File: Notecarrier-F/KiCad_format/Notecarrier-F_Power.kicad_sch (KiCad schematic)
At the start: 0 parts

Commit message: Port Notecarrier-F schematic and BOM.
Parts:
- added C1, C11, C14, C15, C16, C17, C20: 10µF, symbol Device:C
- added C10, C18, C19, C21, C25, C3: 0.1µF, symbol Device:C
- added C12: 47µF, symbol Device:C
- added C13: 4.7µF, symbol Device:C
- added C2: 1µF, symbol Device:C
- added C22, C23, C24: 22µF, symbol Device:C_Small
- added C4: 10000pF, symbol Device:C
- added DS1, DS2, DS4, DS5: FSV1045V, blues-kicad-lib:TO277-3, symbol blues-kicad-lib:FSV1045V
- added DS3, DS6, DS7: STPS3H100U, symbol Device:D_Schottky_Filled
- added J1, J2, J3: S2BPHSM4TBLFSN, symbol Connector_Generic:Conn_01x02
- added J4: 10118193-0001LF, symbol Connector:USB_B_Micro
- added L1: XFL4020-222MEC, symbol Device:L
- added L2: 1.5uH, symbol Device:L
- added L3: 1285AS-H-2R2M=P2, symbol Device:L
- added R1, R2, R4: 10k, symbol Device:R
- added R13: 1.1M, symbol Device:R
- added R14: 180k, symbol Device:R
- added R16: 10MOhms, symbol Device:R
- added R17: 82kOhms, symbol Device:R
- added R3: 470R, symbol Device:R
- added R5: 1M, symbol Device:R
- added TVS1: SM6T6V8A, Diode_SMD:D_SMB, symbol Diode:SM6T6V8A
- added U1: TPS62748YFPT, blues-kicad-lib:XFBGA8, symbol blues-kicad-lib:TPS62748YFPT_NoLabel
- added U2: BQ24210DQCT, blues-kicad-lib:BQ24210DQCT, symbol blues-kicad-lib:BQ24210DQCT
- added U3: TPS63020DSJR, symbol blues-kicad-lib:TPS63020DSJR
- added U5: MAX17225ELT+, blues-kicad-lib:WDFN6-0200X0200, symbol blues-kicad-lib:MAX17225ELT_NoLabel
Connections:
- new net: L1.1, U5.2 (LX)
- new net: R17.1, U5.4 (SEL)
- new net: L2.1, U3.6 (L2-1), U3.7 (L2-2)
- new net: L2.2, U3.8 (L1-2), U3.9 (L1-1)
- new net: C18.1, U3.1 (VINA)
- new net: R3.1, U2.2 (ISET)
- new net: R4.1, U2.4 (VTSB), U2.5 (TS)
- new net: L3.2, U1.A1 (SW)
- new net: C22.1, C23.1, C24.1, C25.1, DS5.1 (A1), DS5.2 (A2), R13.1, U3.4 (VOUT), U3.5 (VOUT)
- new net: DS3.1 (K), DS4.3 (C), U2.1 (VBUS)
- new net: R13.2, R14.1, U3.3 (FB)
- new net: C4.1, J4.6 (Shield), R5.2
- new net: R2.2, U2.6 (~{PG}), U2.7 (~{EN})
- new net 1V8: C14.1, C15.1, C20.1, C21.1, L1.2, L3.1, U1.C2 (VOS), U5.5 (IN), U5.6 (EN)
- new net D_N: J4.2 (D-)
- new net D_P: J4.3 (D+)
- new net EN_F_BAT: U3.12 (EN)
- new net F_BAT: DS5.3 (C)
- new net F_VUSB: DS7.2 (A)
- new net GND: C1.2, C10.2, C11.2, C12.2, C13.2, C14.2, C15.2, C16.2, C17.2, C18.2, C19.2, C2.2, C20.2, C21.2, C22.2, C23.2, C24.2, C25.2, C3.2, C4.2, J1.1 (Pin_1), J2.1 (Pin_1), J3.1 (Pin_1), J4.5 (GND), R14.2, R17.2, R3.2, R4.2, R5.1, TVS1.2 (A2), U1.B2 (GND), U1.D1 (CTRL), U2.11 (EXP), U2.3 (VSS), U3.13 (PS/PSYNC), U3.15 (EXP), U3.2 (GND), U5.3 (GND)
- new net N_AUX5: R1.2, U2.8 (~{CHG})
- new net N_EN: C19.1, R16.2, U1.B1 (EN)
- new net N_VIO: C10.1, C11.1, R1.1, U5.1 (OUT)
- new net V+: DS1.1 (A1), DS1.2 (A2), J1.2 (Pin_2)
- new net VBAT: C2.1, DS2.1 (A1), DS2.2 (A2), J3.2 (Pin_2), R2.1, U2.10 (BAT)
- new net VMAIN: C12.1, C13.1, C16.1, C17.1, DS1.3 (C), DS2.3 (C), DS6.1 (K), DS7.1 (K), R16.1, TVS1.1 (A1), U1.A2 (VIN), U1.C1 (VSEL), U3.10 (VIN), U3.11 (VIN)
- new net VSOLAR: C1.1, DS4.1 (A1), DS4.2 (A2), J2.2 (Pin_2)
- new net VUSB: C3.1, DS3.2 (A), DS6.2 (A), J4.1 (VBUS)
- no-connect marks 0 -> 4
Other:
- note added: "1V8 Power Supply"
- note added: "Feather VBAT Power Supply"
- note added: "Isdmax=1uA"
- note added: "Li-po battery 3.3V - 4.2V"
- note added: "Li-po must be equal to or greater than 800mAh"
- note added: "Main Power Bus"
- note added: "Notecard USB"
- note added: "Notecard VIO Power Supply"
- note added: "Primary Battery"
- note added: "Primary Battery 2.5V - 4.2V"
- note added: "Riset = Kiset / Iiset where Kiset is 395 typically. With 470R --> 800mA"
- note added: "Solar"
- note added: "Solar panel connector"
- note added: "V+"
- title: (none) -> Notecarrier-F

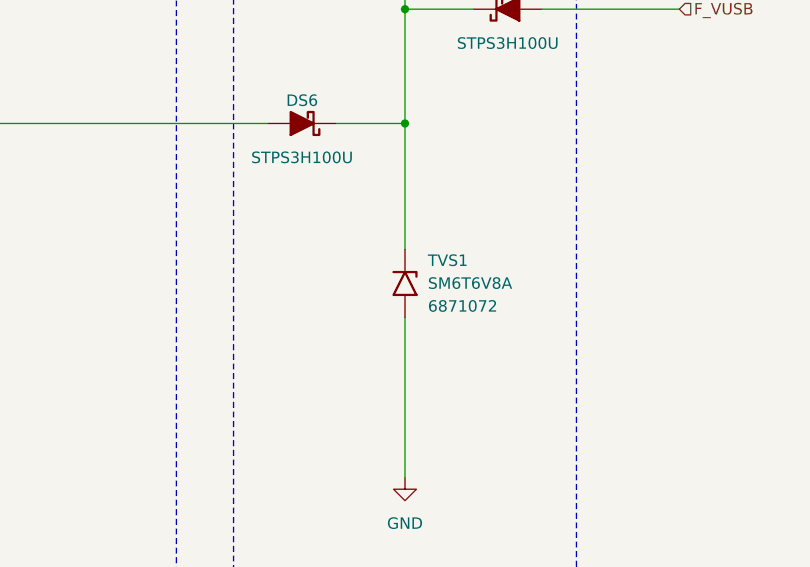
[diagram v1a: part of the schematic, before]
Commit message: Ported footprint assignments, board outline, copper layers and dimensional drawings for Notecarrier-F.
Footprints currently held in a “blues-kicad-lib-pending” library, prior to merging with “blues-kicad-lib” and deleting unused items.
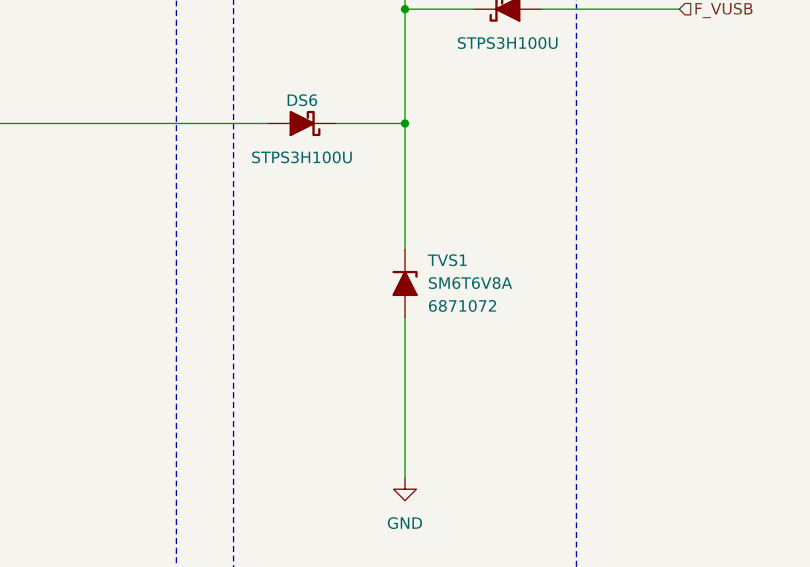
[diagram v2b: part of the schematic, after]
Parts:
- C1, C4: footprint (none) -> blues-kicad-lib-pending:CAP 1206_3216 - 0.8MM
- C10, C11, C14, C15, C18, C19, C2, C20, C21, C25, C3: footprint (none) -> blues-kicad-lib-pending:CAP 0402_1005
- C12: footprint (none) -> blues-kicad-lib-pending:CAP 1210_3225 - 2.8MM
- C13, C16, C17: footprint (none) -> blues-kicad-lib-pending:CAP 0603_1608
- C22, C23, C24: footprint (none) -> blues-kicad-lib-pending:CAP FILM 0805
- DS3, DS6, DS7: footprint (none) -> blues-kicad-lib-pending:DO214AA SMB
- J1, J2, J3: footprint (none) -> blues-kicad-lib-pending:JST S2B-PH-SM4-TB
- J4: footprint (none) -> blues-kicad-lib-pending:FCI USB 10118193-0001LF
- L1: footprint (none) -> blues-kicad-lib-pending:IND_XFL4020-222MEC
- L2: footprint (none) -> blues-kicad-lib-pending:VCHA042A-1R5MS6
- L3: footprint (none) -> blues-kicad-lib-pending:1285AS-H-2R2M=P2-INDC2016X100N
- R1, R13, R14, R16, R17, R2, R3, R4: footprint (none) -> blues-kicad-lib-pending:RES 0402_1005
- R5: footprint (none) -> blues-kicad-lib-pending:RES 1206_3216
- TVS1: footprint Diode_SMD:D_SMB -> blues-kicad-lib-pending:SMB_Backwards; symbol Diode:SM6T6V8A -> blues-kicad-lib:SM6T6V8A
- U1: footprint blues-kicad-lib:XFBGA8 -> blues-kicad-lib-pending:TPS62748YFPT-DSBGA4x2
- U3: footprint (none) -> blues-kicad-lib-pending:TI PVSON-14 DSJ
- U5: footprint blues-kicad-lib:WDFN6-0200X0200 -> blues-kicad-lib-pending:MAX17225ELT+UDFN

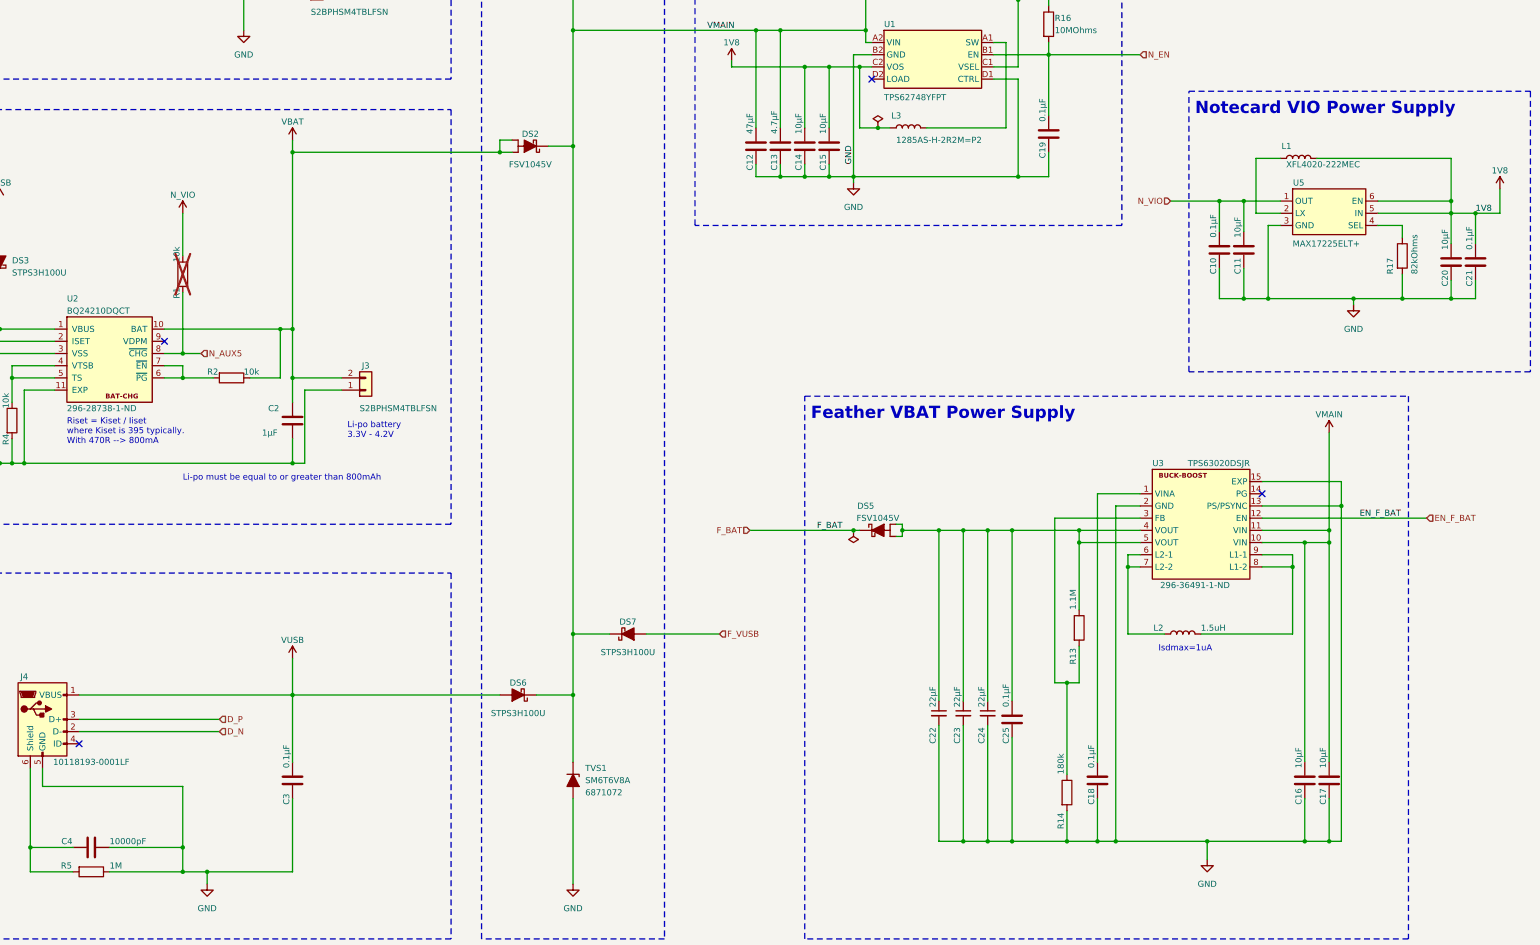
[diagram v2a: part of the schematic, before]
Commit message: Finish first pass PCB port.
Still need to go back and finalise top-level schematic sheet.
Next step is validation where there’s bound to be lots of copper rules to tweak.
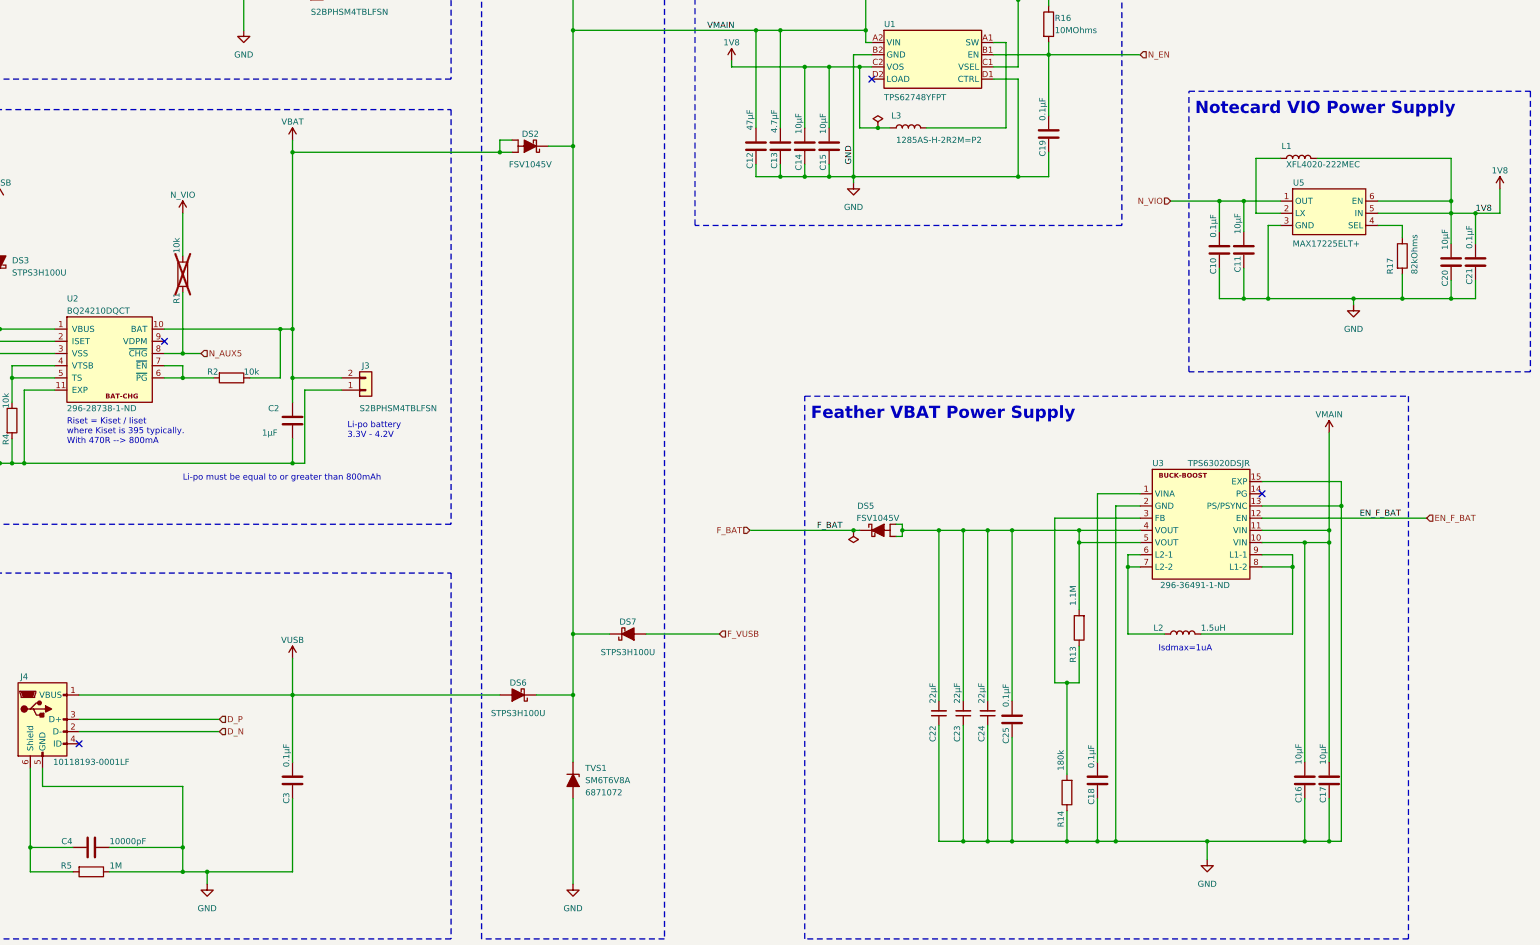
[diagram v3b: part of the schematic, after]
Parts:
- DS3, DS6, DS7: symbol Device:D_Schottky_Filled -> blues-kicad-lib:D_Schottky_Filled_Swapped
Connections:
- net 1V8: now also C21.2; no longer C21.1
- net F_VUSB: now also DS7.1 (A); no longer DS7.2 (A)
- net GND: now also C11.1, C12.1, C13.1, C16.1, C17.1, C19.1, C21.1, C22.1, C23.1, C24.1, C3.1, C4.1, R14.1; no longer C11.2, C12.2, C13.2, C16.2, C17.2, C19.2, C21.2, C22.2, C23.2, C24.2, C3.2, C4.2, R14.2
- net N_AUX5: now also R1.1; no longer R1.2
- net N_EN: now also C19.2; no longer C19.1
- net N_VIO: now also C11.2, R1.2; no longer C11.1, R1.1
- net VMAIN: now also C12.2, C13.2, C16.2, C17.2, DS6.2 (K), DS7.2 (K); no longer C12.1, C13.1, C16.1, C17.1, DS6.1 (K), DS7.1 (K)
- net VUSB: now also C3.2, DS3.1 (A), DS6.1 (A); no longer C3.1, DS3.2 (A), DS6.2 (A)
- net at C25.1, DS5.1 (A1), DS5.2 (A2)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: now also C22.2, C23.2, C24.2, R13.2; no longer C22.1, C23.1, C24.1, R13.1
- net at DS4.3 (C), U2.1 (VBUS): now also DS3.2 (K); no longer DS3.1 (K)
- net at J4.6 (Shield), R5.2: now also C4.2; no longer C4.1
- new net: R13.1, R14.2, U3.3 (FB)
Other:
- moved on the sheet: C11, C12, C13, C16, C17, C19, C21, C22, C23, C24, C3, C4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

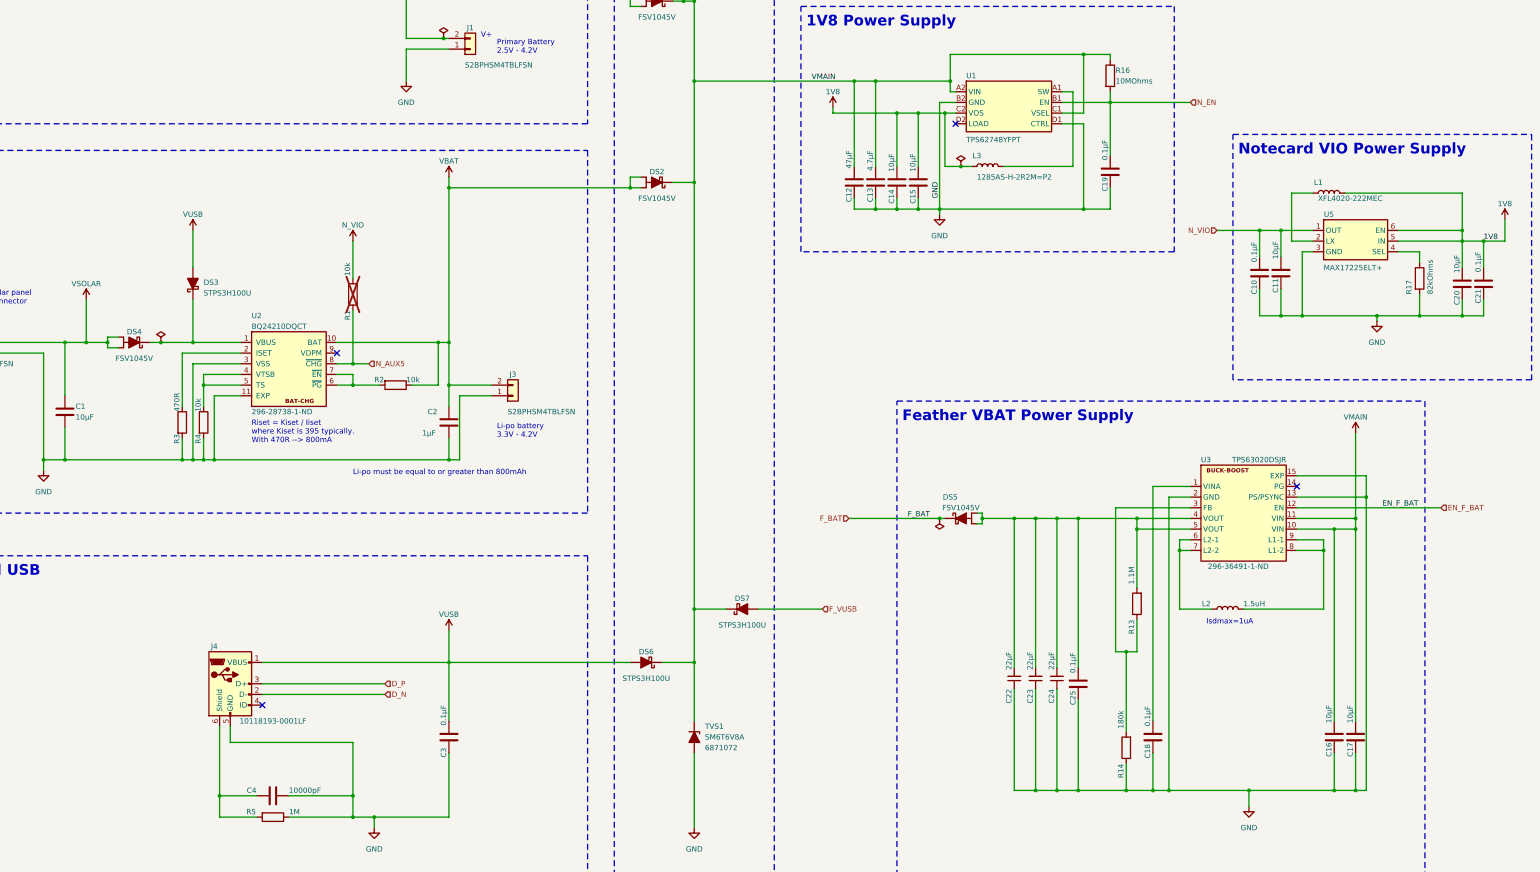
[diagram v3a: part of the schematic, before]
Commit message: Apply first pass validation of Notecarrier-F port
Huge push to identify, solve, document and revalidate all the details revealed by the first run of the validation process. Validation is now acceptable and preparation can be made to release Rev A.
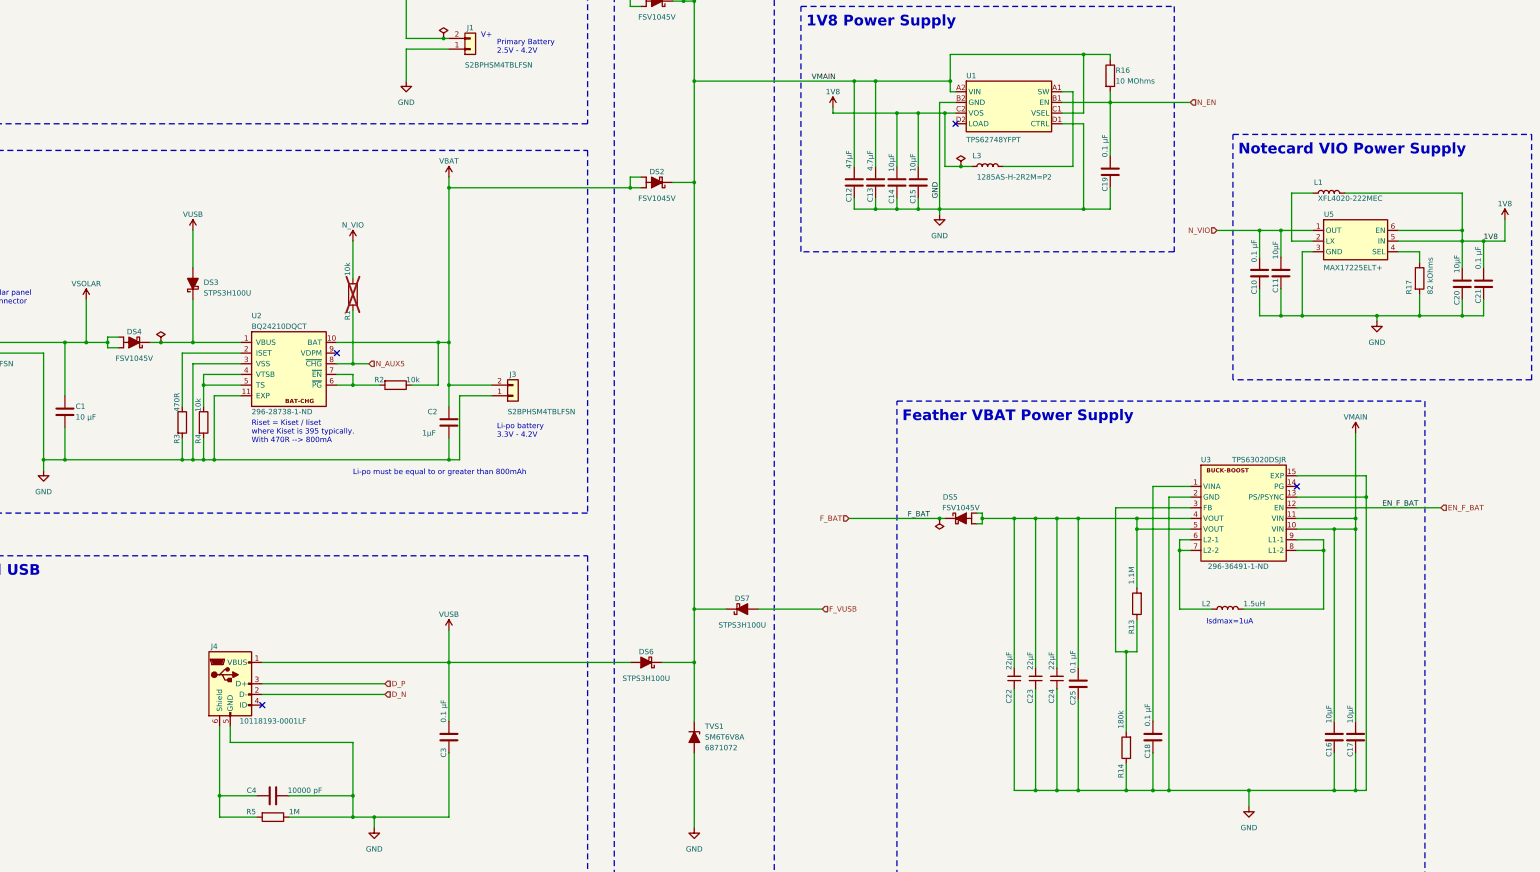
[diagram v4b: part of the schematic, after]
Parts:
- C1: value 10µF -> 10 µF; Manufacturer Samsung -> Sams
- C10, C18, C19, C21, C25, C3: value 0.1µF -> 0.1 µF
- C4: value 10000pF -> 10000 pF
- R16: value 10MOhms -> 10 MOhms
- R17: value 82kOhms -> 82 kOhms
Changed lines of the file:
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@@
       (effects (font (size 1.27 1.27)) (justify left))
     )
-    (property "Value" "0.1µF" (at 312.42 217.17 90)
+    (property "Value" "0.1 µF" (at 312.42 217.17 90)
       (effects (font (size 1.27 1.27)) (justify left))
     )
@@
       (effects (font (size 1.27 1.27)) (justify left))
     )
-    (property "Value" "10MOhms" (at 304.8 63.5 0)
+    (property "Value" "10 MOhms" (at 304.8 63.5 0)
       (effects (font (size 1.27 1.27)) (justify left))
     )
@@
       (effects (font (size 1.27 1.27)) (justify left))
     )
-    (property "Value" "0.1µF" (at 294.64 204.47 90)
+    (property "Value" "0.1 µF" (at 294.64 204.47 90)
       (effects (font (size 1.27 1.27)) (justify left))
     )
@@
       (effects (font (size 1.27 1.27)) (justify left))
     )
-    (property "Value" "0.1µF" (at 391.16 104.14 90)
+    (property "Value" "0.1 µF" (at 391.16 102.87 90)
       (effects (font (size 1.27 1.27)) (justify left))
     )
@@
       (effects (font (size 1.27 1.27)) (justify left))
     )
-    (property "Value" "0.1µF" (at 337.82 106.68 90)
+    (property "Value" "0.1 µF" (at 337.82 106.68 90)
       (effects (font (size 1.27 1.27)) (justify left))
     )
@@
       (effects (font (size 1.27 1.27)) (justify left))
     )
-    (property "Value" "0.1µF" (at 302.26 77.47 90)
+    (property "Value" "0.1 µF" (at 302.26 76.2 90)
       (effects (font (size 1.27 1.27)) (justify left))
     )
@@
       (effects (font (size 1.27 1.27)))
     )
-    (property "Value" "10000pF" (at 111.76 232.41 90)
+    (property "Value" "10000 pF" (at 111.76 232.41 90)
       (effects (font (size 1.27 1.27)))
     )
@@
       (effects (font (size 1.27 1.27)) (justify left))
     )
-    (property "Value" "82kOhms" (at 379.73 114.3 90)
+    (property "Value" "82 kOhms" (at 379.73 114.3 90)
       (effects (font (size 1.27 1.27)) (justify left))
     )
@@
       (effects (font (size 1.27 1.27)) (justify left))
     )
-    (property "Value" "0.1µF" (at 144.78 212.09 90)
+    (property "Value" "0.1 µF" (at 144.78 210.82 90)
       (effects (font (size 1.27 1.27)) (justify left))
     )
@@
       (effects (font (size 1.27 1.27)) (justify left))
     )
-    (property "Value" "10µF" (at 57.15 143.51 0)
+    (property "Value" "10 µF" (at 57.15 143.51 0)
       (effects (font (size 1.27 1.27)) (justify left))
     )
@@
       (effects (font (size 1.27 1.27)) hide)
     )
-    (property "Manufacturer" "Samsung" (at 54.61 142.24 0)
-      (effects (font (size 1.27 1.27)) hide)
-    )
+    (property "Manufacturer" "Sams" (at 54.61 142.24 0)
+      (effects (font (size 1.27 1.27)) hide)
+    )
